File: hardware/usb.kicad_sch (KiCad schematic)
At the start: 35 parts, among them J3 USB_C_Receptacle_USB2.0_14P, J4 USB_C_Receptacle_USB2.0_14P, J5 USB_C_Receptacle_USB2.0_14P, J6 USB_A_Stacked, U10 TPD2EUSB30, U11 TPD2EUSB30, U12 TPD2EUSB30, U13 SY6280AAC, U14 SY6280AAC, U16 TPD2EUSB30, U6 HUSB237, U7 SY6280AAC, U8 SY6280AAC, U9 TPD2EUSB30

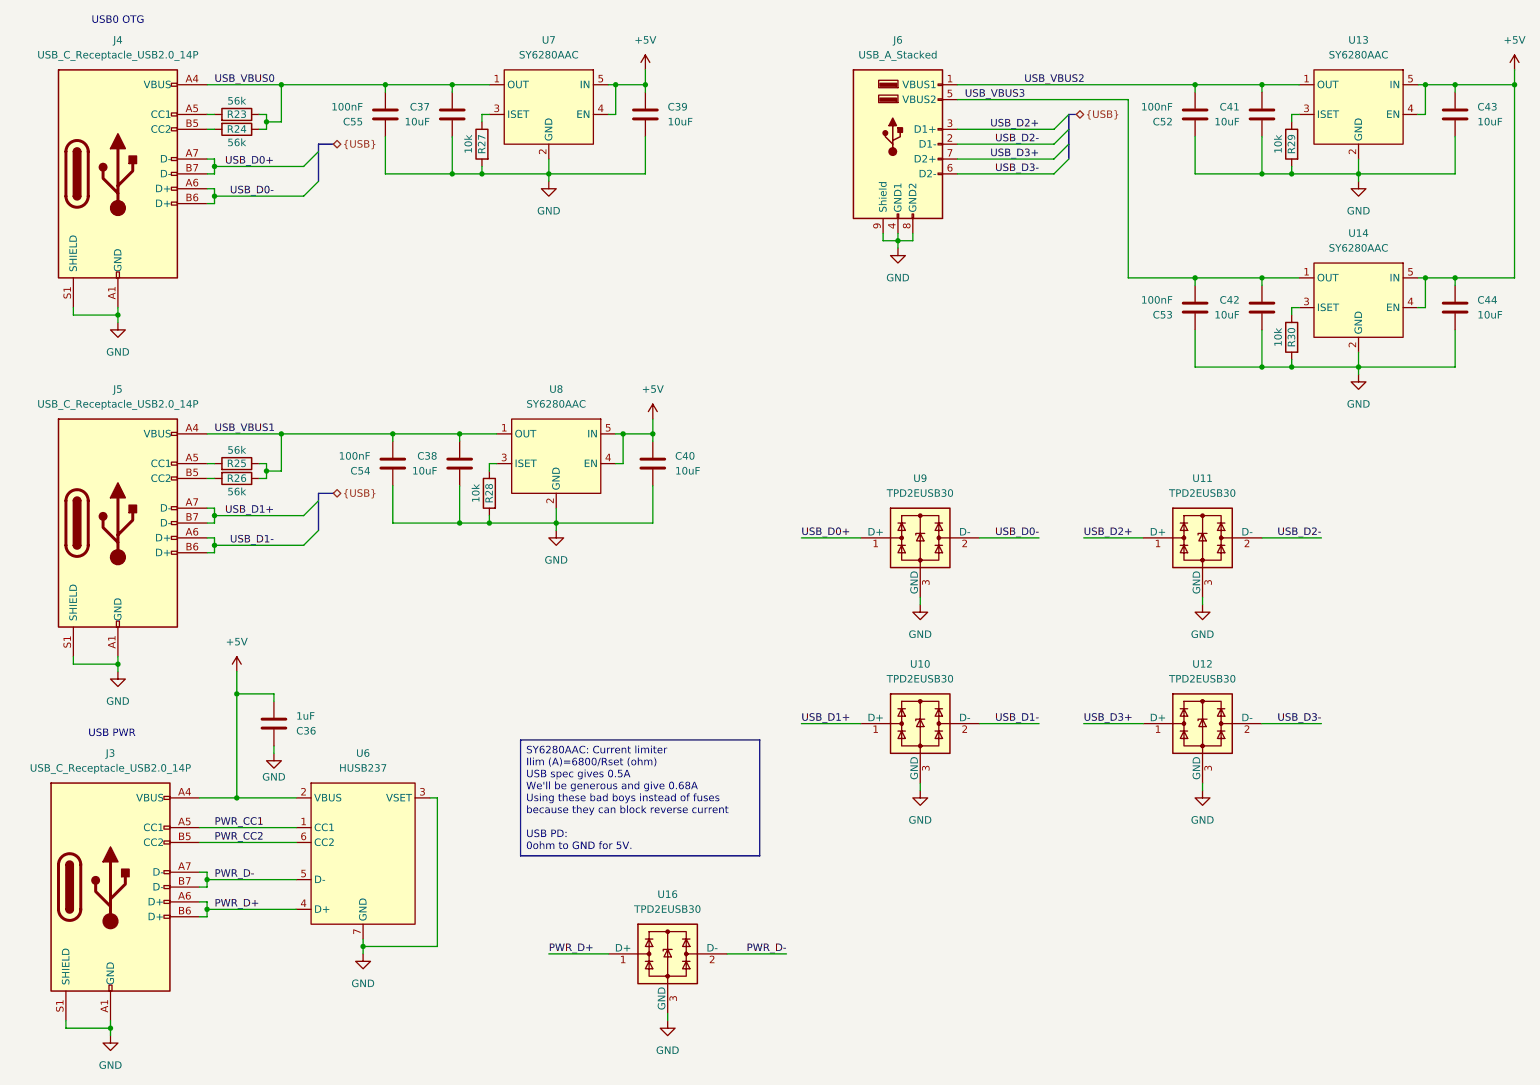
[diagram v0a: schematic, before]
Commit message: Finished DC DC converters and started decoupling the CPU
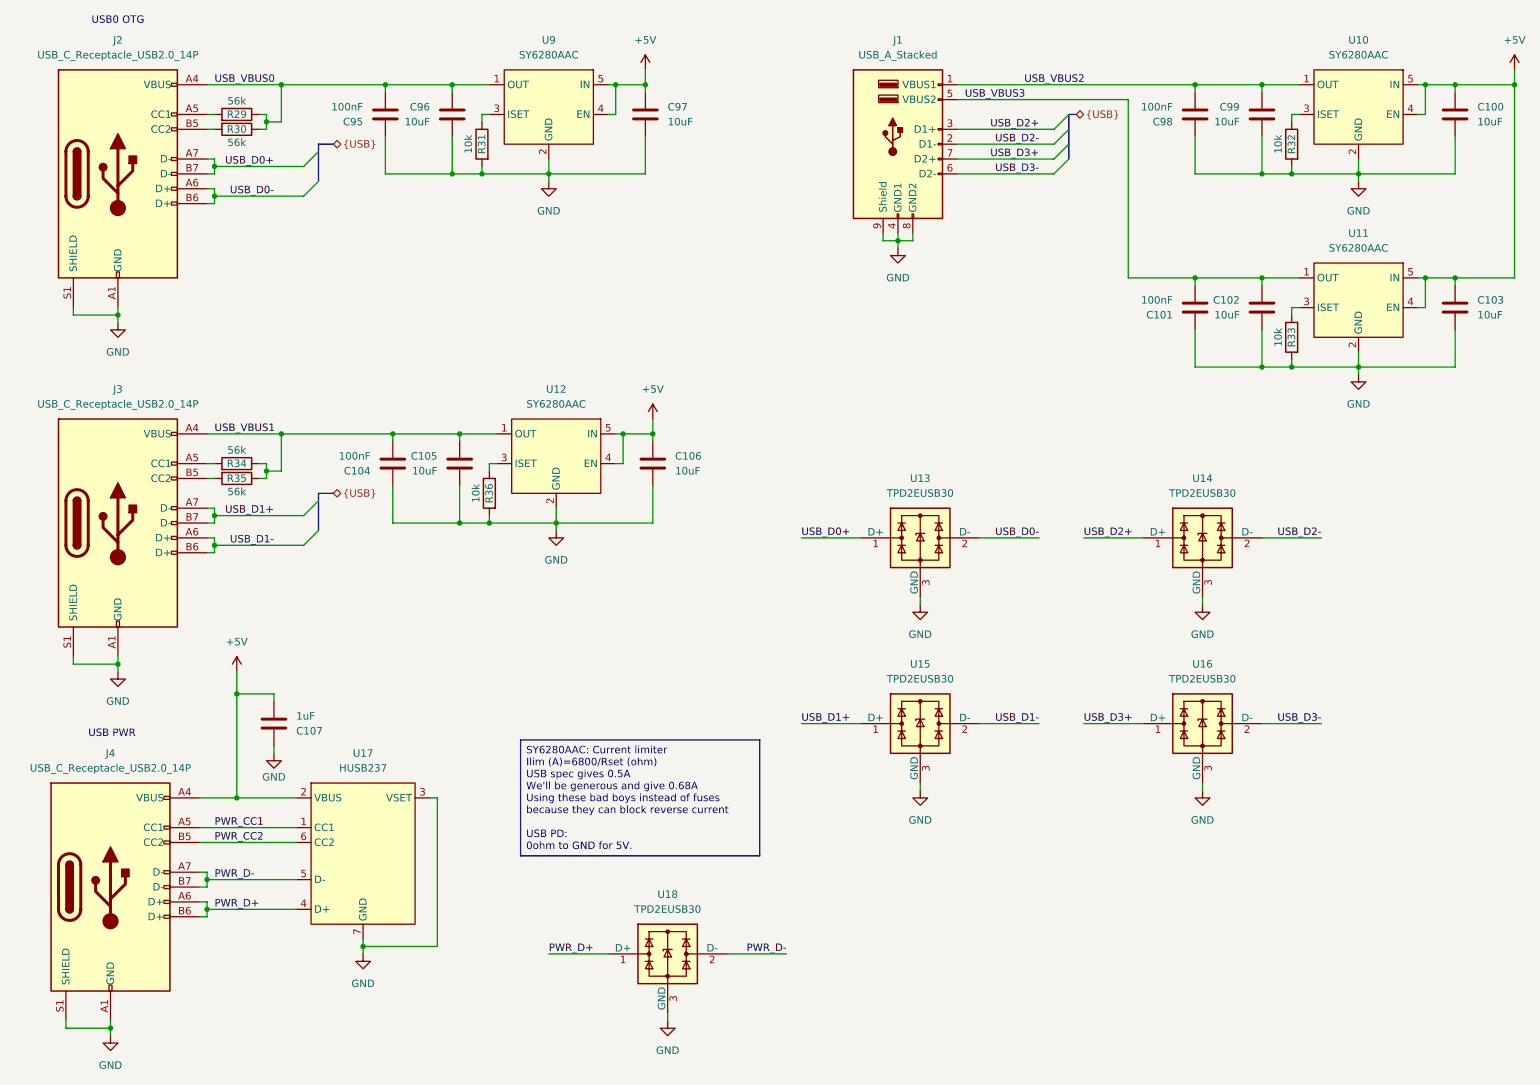
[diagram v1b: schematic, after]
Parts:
- renumbered C43 to C100, C53 to C101, C42 to C102, C44 to C103, C54 to C104, C38 to C105, C40 to C106, C36 to C107, C55 to C95, C37 to C96, C39 to C97, C52 to C98, C41 to C99, J6 to J1, J4 to J2, J5 to J3, J3 to J4, R23 to R29, R24 to R30, R27 to R31, R29 to R32, R30 to R33, R25 to R34, R26 to R35, R28 to R36, U13 to U10, U14 to U11, U8 to U12, U9 to U13, U11 to U14, U10 to U15, U12 to U16, U6 to U17, U16 to U18, U7 to U9

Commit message: Decoupling on PCB side almost done
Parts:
- J2, J3, J4: FT Position Offset (none) -> 0,12.7
- U10, U11, U12, U17, U9: FT Rotation Offset (none) -> 90
- U13, U14, U15, U16, U18: FT Rotation Offset (none) -> -90
